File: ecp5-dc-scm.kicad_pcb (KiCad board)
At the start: 8 copper layers, 90 x 120.4 mm, 463 parts, among them IC1 TPS54561, J1 L834-1G1T-S7, J2 1-2199230-6, J3 529910408, J4 M20-7830642, J5 SFF-TA-1002-4C+, J6 0878311420, J7 61300611121, J8 S2B-PH-K-S_LF__SN_, Q1 2N7002, Q10 2N7002, Q11 2N7002, Q12 2N7002, Q13 2N7002, Q14 2N7002, Q15 2N7002, Q16 2N7002, Q17 2N7002, Q2 2N7002, Q3 2N7002, Q4 IRLML6402TRPBF, Q5 IRLML6402TRPBF, Q6 IRLML6402TRPBF, Q7 IRLML6402TRPBF, Q8 IRLML6402TRPBF, Q9 IRLML6402TRPBF, U1 KSZ9031RNXCA, U10 AS4C256M16D3, U11 TPS51200DRC, U12 LM3881MME_NOPB, U13 LM21212-2, U14 SN74LVC1G11DBVR, U16 TPS62823DLCT, U17 TPS62823DLCT, U18 TPS62823DLCT, U19 TPS62823DLCT, U2 W25Q32JVSSIQ_TR, U20 TPS62823DLCT, U21 ECP5UM5G_85_CABGA756, U3 W25Q32JVSSIQ_TR, U4 W25Q32JVSSIQ_TR, U5 W25Q32JVSSIQ_TR, U6 MTFC32GAPALBH-AIT, U7 NVT2008DQ,115, U8 USB3300-EZK-TR, U9 USB3300-EZK-TR, Y1 ABM8G-25.000MHZ-18-D2Y-T, Y2 TSX-3225, Y3 TSX-3225

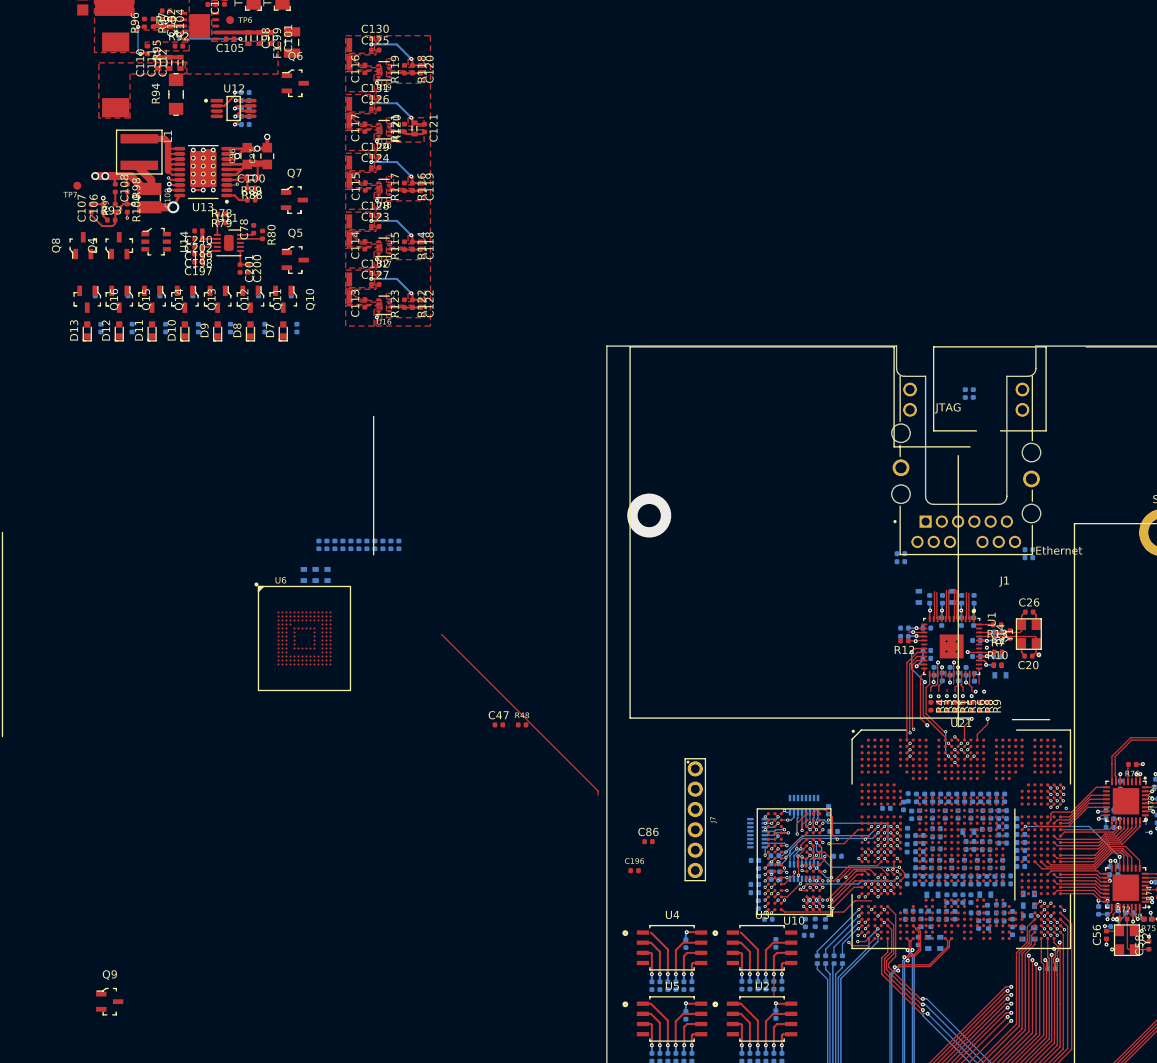
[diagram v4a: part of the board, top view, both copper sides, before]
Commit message: I3C routed
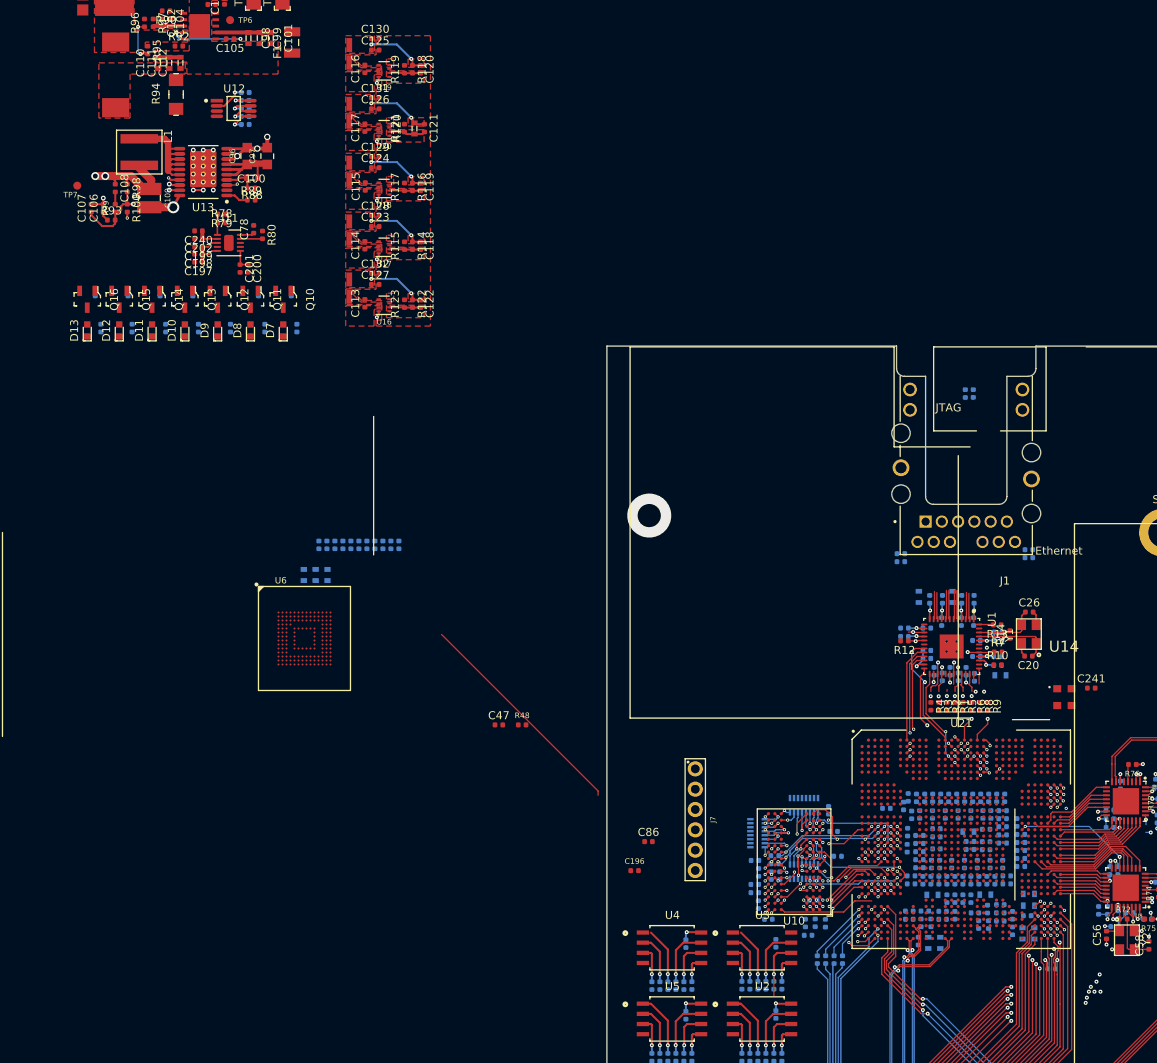
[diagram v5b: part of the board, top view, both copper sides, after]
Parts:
- removed Q4, Q5, Q6, Q7, Q8, Q9: IRLML6402TRPBF, ecp5-dc-scm-footprints:SOT-23-3
- added C241: C_100n_0402, ecp5-dc-scm-footprints:0402-cap, F.Cu at (120.7, 101.7)
- U14: value SN74LVC1G11DBVR -> AMJMEFB-100.0000T; footprint ecp5-dc-scm-footprints:SOT-23-6 -> antmicro-footprints:AMJMEFB
- moved U14 126.9 mm to (117.2, 102.5), turned to 0 degrees
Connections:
- net /Power supply/VR2_PG renamed GCLK100
- C154 pad 1: VCC -> VCC1V2
- C156 pad 1: VCC -> VCC1V2
- C159 pad 1: VCC -> VCC1V2
- C162 pad 1: VCC -> VCC1V2
- C165 pad 1: VCC -> VCC1V2
- C168 pad 1: VCC -> VCC1V2
- C171 pad 1: VCC -> VCC1V2
- C174 pad 1: VCC -> VCC1V2
- C177 pad 1: VCC -> VCC1V2
- C181 pad 1: VCC -> VCC1V2
- C183 pad 1: VCC -> VCC1V2
- C185 pad 1: VCC -> VCC1V2
- C187 pad 1: VCC -> VCC1V2
- C188 pad 1: VCC -> VCC1V2
- C189 pad 1: VCC -> VCC1V2
- C190 pad 1: VCC -> VCC1V2
- C191 pad 1: VCC -> VCC1V2
- C192 pad 1: VCC -> VCC1V2
- C193 pad 1: VCC -> VCC1V2
- C194 pad 1: VCC -> VCC1V2
- C195 pad 1: VCC -> VCC1V2
- C203 pad 1: VCC3V3_T -> VCC3V3
- C204 pad 1: VCC3V3_T -> VCC3V3
- C205 pad 1: VCC3V3_T -> VCC3V3
- C206 pad 1: VCC3V3_T -> VCC3V3
- C207 pad 1: VCC3V3_T -> VCC3V3
- C209 pad 1: VCC3V3_T -> VCC3V3
- C210 pad 1: VCC3V3_T -> VCC3V3
- C211 pad 1: VCC3V3_T -> VCC3V3
- C212 pad 1: VCC3V3_T -> VCC3V3
- C213 pad 1: VCC3V3_T -> VCC3V3
- C214 pad 1: VCC3V3_T -> VCC3V3
- C215 pad 1: VCC3V3_T -> VCC3V3
- C218 pad 1: VCC3V3_T -> VCC3V3
- C219 pad 1: VCC1V8_T -> VCC1V8
- C220 pad 1: VCC3V3_T -> VCC3V3
- C221 pad 1: VCC1V8_T -> VCC1V8
- C222 pad 1: VCC1V8_T -> VCC1V8
- C223 pad 1: VCC1V8_T -> VCC1V8
- C224 pad 1: VCC1V8_T -> VCC1V8
- C225 pad 1: VCC3V3_T -> VCC3V3
- C226 pad 1: VCC3V3_T -> VCC3V3
- C227 pad 1: VCC3V3_T -> VCC3V3
- C228 pad 1: VCC3V3_T -> VCC3V3
- C229 pad 1: VCC3V3_T -> VCC3V3
- C230 pad 1: VCC1V35_T -> VCC1V35
- C231 pad 1: VCC1V35_T -> VCC1V35
- C232 pad 1: VCC1V35_T -> VCC1V35
- C233 pad 1: VCC1V35_T -> VCC1V35
- C234 pad 1: VCC1V35_T -> VCC1V35
- C235 pad 1: VCC3V3_T -> VCC3V3
- C236 pad 1: VCC3V3_T -> VCC3V3
- C237 pad 1: VCC3V3_T -> VCC3V3
- C238 pad 1: VCC3V3_T -> VCC3V3
- C239 pad 1: VCC3V3_T -> VCC3V3
- FB4 pad 1: VCC -> VCC1V2
- FB5 pad 1: VCC -> VCC1V2
- FB6 pad 1: VCC -> VCC1V2
- FB7 pad 2: VCC -> VCC1V2
- FB8 pad 2: VCC2V5_T -> VCC2V5
- J7 pad 1: VCC -> VCC3V3
- R126 pad 2: VCC3V3_T -> VCC3V3
- R127 pad 2: VCC3V3_T -> VCC3V3
- R129 pad 1: VCC3V3_T -> VCC3V3
- R130 pad 1: VCC3V3_T -> VCC3V3
- R131 pad 2: VCC3V3_T -> VCC3V3
- R84 pad 1: VCC3V3 -> VCC5V0
- R85 pad 1: VCC3V3 -> VCC5V0
- R85 pad 2: /Power supply/VCCINT_EN -> /Power supply/VCCA0_EN
- R86 pad 1: VCC3V3 -> VCC5V0
- R86 pad 2: /Power supply/VCCAUX_EN -> /Power supply/VCCIO_EN
- R87 pad 1: VCC3V3 -> VCC5V0
- R87 pad 2: /Power supply/VCCIO_EN -> /Power supply/VCCAUX_EN
- U12 pad 1: VCC3V3 -> VCC5V0
- U12 pad 4: VCC3V3 -> VCC5V0
- U12 pad 6: /Power supply/VCCIO_EN -> /Power supply/VCCAUX_EN
- U12 pad 7: /Power supply/VCCAUX_EN -> /Power supply/VCCIO_EN
- U12 pad 8: /Power supply/VCCINT_EN -> /Power supply/VCCA0_EN
- U13 pad 3: /Power supply/1V2_EN -> /Power supply/VCCA0_EN
- U14 pad 1: /Power supply/VR1_PG -> VCC3V3
- U14 pad 4: /Power supply/VR_GOOD -> VCC3V3_T
- U16 pad 1: VCC5V0 -> /Power supply/VCCAUX_EN
- U17 pad 1: VCC5V0 -> /Power supply/VCCIO_EN
- U18 pad 1: VCC5V0 -> /Power supply/VCCIO_EN
- U19 pad 1: VCC5V0 -> /Power supply/VCCIO_EN
- U20 pad 1: VCC5V0 -> /Power supply/VCCA0_EN
- U21 pad A20: Net-(U21-PadA20) -> I3C[0]_SCL_3V3
- U21 pad A22: I3C[2]_SCL_3V3 -> Net-(U21-PadA22)
- U21 pad A23: I3C[0]_SDA_3V3 -> Net-(U21-PadA23)
- U21 pad AA10: VCC1V35_T -> VCC1V35
- U21 pad AA12: VCC -> VCC1V2
- U21 pad AA13: VCC -> VCC1V2
- U21 pad AA14: VCC -> VCC1V2
- U21 pad AA15: VCC -> VCC1V2
- U21 pad AA16: VCC -> VCC1V2
- U21 pad AA17: VCC -> VCC1V2
- U21 pad AA18: VCC -> VCC1V2
- U21 pad AA19: VCC -> VCC1V2
- U21 pad AA20: VCC -> VCC1V2
- U21 pad AA21: VCC -> VCC1V2
- U21 pad AA23: VCC3V3_T -> VCC3V3
- U21 pad AB10: VCC3V3_T -> VCC3V3
- U21 pad AB23: VCC3V3_T -> VCC3V3
- U21 pad AC10: VCC3V3_T -> VCC3V3
- U21 pad AC23: VCC3V3_T -> VCC3V3
- U21 pad B22: I3C[1]_SCL_3V3 -> Net-(U21-PadB22)
- U21 pad C19: Net-(U21-PadC19) -> I3C[0]_SDA_3V3
- U21 pad C20: I3C[3]_SCL_3V3 -> I3C[3]_SDA_3V3
- U21 pad C22: I3C[2]_SDA_3V3 -> Net-(U21-PadC22)
- U21 pad D19: Net-(U21-PadD19) -> I3C[1]_SDA_3V3
- U21 pad D20: Net-(U21-PadD20) -> I3C[3]_SCL_3V3
- U21 pad D22: I3C[1]_SDA_3V3 -> Net-(U21-PadD22)
- U21 pad D32: Net-(U21-PadD32) -> ESPI_RESET_N
- U21 pad E19: Net-(U21-PadE19) -> I3C[2]_SCL_3V3
- U21 pad E22: I3C[0]_SCL_3V3 -> Net-(U21-PadE22)
- U21 pad E32: Net-(U21-PadE32) -> ESPI_IO2
- U21 pad F19: Net-(U21-PadF19) -> I3C[2]_SDA_3V3
- U21 pad F20: I3C[3]_SDA_3V3 -> I3C[1]_SCL_3V3
- U21 pad F31: Net-(U21-PadF31) -> ESPI_ALERT_N
- U21 pad F32: Net-(U21-PadF32) -> ESPI_IO3
- U21 pad H30: ESPI_RESET_N -> ESPI_CS0_N
- U21 pad H31: ESPI_IO3 -> ESPI_IO0
- U21 pad H32: ESPI_CS1_N -> ESPI_IO1
- U21 pad J30: Net-(U21-PadJ30) -> ESPI_CS1_N
- U21 pad J32: ESPI_IO2 -> Net-(U21-PadJ32)
- U21 pad K12: VCC3V3_T -> VCC3V3
- U21 pad K14: VCC3V3_T -> VCC3V3
- U21 pad K15: VCC3V3_T -> VCC3V3
- U21 pad K16: VCC3V3_T -> VCC3V3
- U21 pad K17: VCC3V3_T -> VCC3V3
- U21 pad K18: VCC3V3_T -> VCC3V3
- U21 pad K19: VCC3V3_T -> VCC3V3
- U21 pad K21: VCC3V3_T -> VCC3V3
- U21 pad K30: ESPI_ALERT_N -> ESPI_CLK
- U21 pad K31: ESPI_IO1 -> Net-(U21-PadK31)
- U21 pad K32: ESPI_IO0 -> Net-(U21-PadK32)
- U21 pad L31: ESPI_CLK -> Net-(U21-PadL31)
- U21 pad L32: ESPI_CS0_N -> Net-(U21-PadL32)
- U21 pad M10: VCC3V3_T -> VCC3V3
- U21 pad M12: VCC -> VCC1V2
- U21 pad M13: VCC -> VCC1V2
- U21 pad M14: VCC -> VCC1V2
- U21 pad M15: VCC -> VCC1V2
- U21 pad M16: VCC -> VCC1V2
- U21 pad M17: VCC -> VCC1V2
- U21 pad M18: VCC -> VCC1V2
- U21 pad M19: VCC -> VCC1V2
- U21 pad M20: VCC -> VCC1V2
- U21 pad M21: VCC -> VCC1V2
- U21 pad M23: VCC1V8_T -> VCC1V8
- U21 pad N12: VCC -> VCC1V2
- U21 pad N21: VCC -> VCC1V2
- U21 pad P10: VCC3V3_T -> VCC3V3
- U21 pad P12: VCC -> VCC1V2
- U21 pad P21: VCC -> VCC1V2
- U21 pad P23: VCC1V8_T -> VCC1V8
- U21 pad R10: VCC3V3_T -> VCC3V3
- U21 pad R12: VCC -> VCC1V2
- U21 pad R21: VCC -> VCC1V2
- U21 pad R23: VCC1V8_T -> VCC1V8
- U21 pad T10: VCC3V3_T -> VCC3V3
- U21 pad T12: VCC -> VCC1V2
- U21 pad T21: VCC -> VCC1V2
- U21 pad T23: VCC1V8_T -> VCC1V8
- U21 pad U10: VCC1V35_T -> VCC1V35
- U21 pad U12: VCC -> VCC1V2
- U21 pad U21: VCC -> VCC1V2
- U21 pad U23: VCC3V3_T -> VCC3V3
- U21 pad V10: VCC1V35_T -> VCC1V35
- U21 pad V12: VCC -> VCC1V2
- U21 pad V21: VCC -> VCC1V2
- U21 pad V23: VCC3V3_T -> VCC3V3
- U21 pad W10: VCC1V35_T -> VCC1V35
- U21 pad W12: VCC -> VCC1V2
- U21 pad W21: VCC -> VCC1V2
- U21 pad W23: VCC3V3_T -> VCC3V3
- U21 pad Y12: VCC -> VCC1V2
- U21 pad Y21: VCC -> VCC1V2
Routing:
- net UART1_SCM_RX: track 113.0 -> 65.2 mm
- net UART0_SCM_TX: track 112.2 -> 64.4 mm
- net UART1_SCM_TX: track 113.3 -> 65.6 mm
- net UART0_SCM_RX: track 111.9 -> 64.1 mm
- net ESPI_CS1_N: track 126.0 -> 78.5 mm, vias 2 -> 3
- net I3C[2]_SDA_3V3: track 88.3 -> 72.2 mm, vias 1 -> 3
- net I3C[1]_SCL_3V3: track 87.0 -> 71.2 mm, vias 1 -> 3
- net I3C[2]_SCL_3V3: track 87.2 -> 72.1 mm, vias 1 -> 3
- net I3C[1]_SDA_3V3: track 87.7 -> 73.2 mm, vias 1 -> 3
- net I3C[3]_SCL_3V3: track 88.4 -> 74.6 mm, vias 1 -> 3
- net I3C[0]_SDA_3V3: track 87.5 -> 75.1 mm, vias 1 -> 3
- net I3C[3]_SDA_3V3: track 89.5 -> 77.5 mm, vias 1 -> 3
- net I3C[0]_SCL_3V3: track 87.7 -> 76.4 mm, vias 1 -> 3
- net /Power supply/VCCA0_EN: track 0.00 -> 4.00 mm, vias 0 -> 2
- net /Power supply/VCCINT_EN: track 2.58 -> 0.00 mm, vias 1 -> 0
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
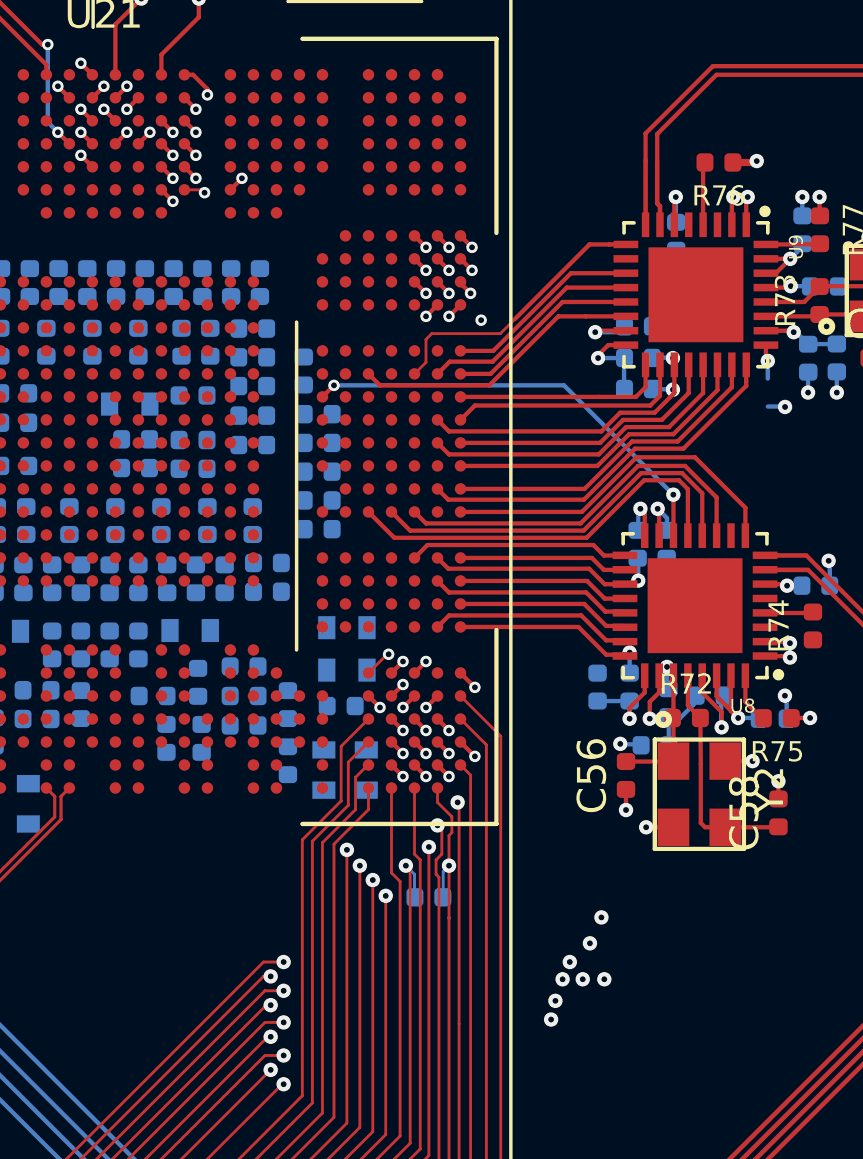
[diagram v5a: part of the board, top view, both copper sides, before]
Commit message: UART routed, fixed ESPI pins
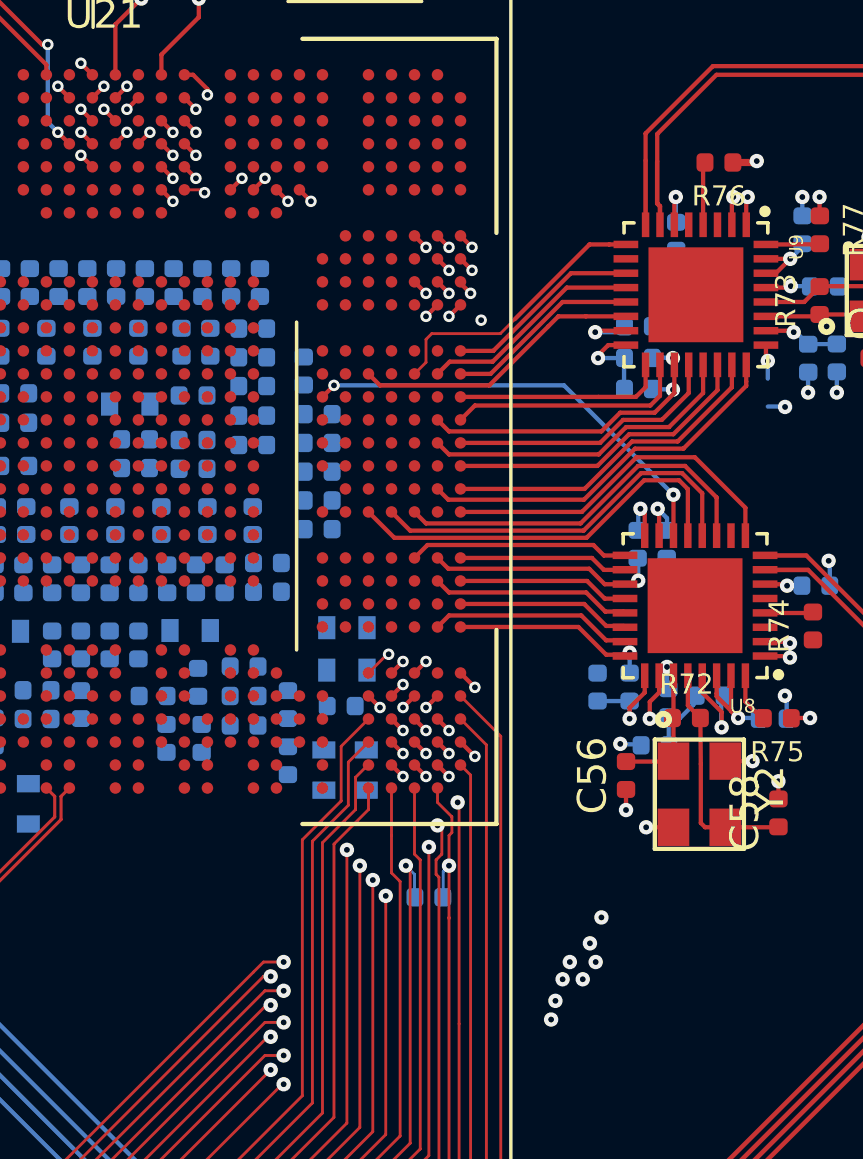
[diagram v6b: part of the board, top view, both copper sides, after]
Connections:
- U21 pad A23: Net-(U21-PadA23) -> I2C[10]_SDA
- U21 pad B22: Net-(U21-PadB22) -> I2C[8]_SDA
- U21 pad D22: Net-(U21-PadD22) -> I2C[4]_SCL
- U21 pad D32: ESPI_RESET_N -> Net-(U21-PadD32)
- U21 pad E22: Net-(U21-PadE22) -> I2C[12]_SCL
- U21 pad E32: ESPI_IO2 -> Net-(U21-PadE32)
- U21 pad F22: I2C[12]_SCL -> UART1_SCM_TX
- U21 pad F23: I2C[10]_SDA -> UART1_SCM_RX
- U21 pad F24: I2C[8]_SDA -> UART0_SCM_TX
- U21 pad F25: I2C[4]_SCL -> UART0_SCM_RX
- U21 pad F31: ESPI_ALERT_N -> Net-(U21-PadF31)
- U21 pad F32: ESPI_IO3 -> Net-(U21-PadF32)
- U21 pad H30: ESPI_CS0_N -> ESPI_RESET_N
- U21 pad H31: ESPI_IO0 -> ESPI_IO3
- U21 pad H32: ESPI_IO1 -> ESPI_CS1_N
- U21 pad J30: ESPI_CS1_N -> Net-(U21-PadJ30)
- U21 pad J32: Net-(U21-PadJ32) -> ESPI_IO2
- U21 pad K30: ESPI_CLK -> ESPI_ALERT_N
- U21 pad K31: Net-(U21-PadK31) -> ESPI_IO1
- U21 pad K32: Net-(U21-PadK32) -> ESPI_IO0
- U21 pad L31: Net-(U21-PadL31) -> ESPI_CLK
- U21 pad L32: Net-(U21-PadL32) -> ESPI_CS0_N
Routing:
- net UART1_SCM_TX: track 65.6 -> 103.3 mm, vias 1 -> 2
- net UART1_SCM_RX: track 65.2 -> 102.9 mm, vias 1 -> 2
- net UART0_SCM_TX: track 64.4 -> 101.3 mm, vias 1 -> 2
- net UART0_SCM_RX: track 64.1 -> 100.6 mm, vias 1 -> 2
- net I2C[12]_SCL: track 93.1 -> 92.5 mm, vias 2 -> 1
- net ESPI_CS1_N: track 78.5 -> 77.9 mm, vias 3 -> 2
